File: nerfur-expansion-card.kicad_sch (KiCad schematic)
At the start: 12 parts, among them J1 RJ45, J10 AudioJack4, J11 HDMI_A, J2 Micro_SD_Card, J3 RJ45, J4 Micro_SD_Card, J5 USB_A, J6 USB_A, J7 USB_A, J8 HDMI_A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

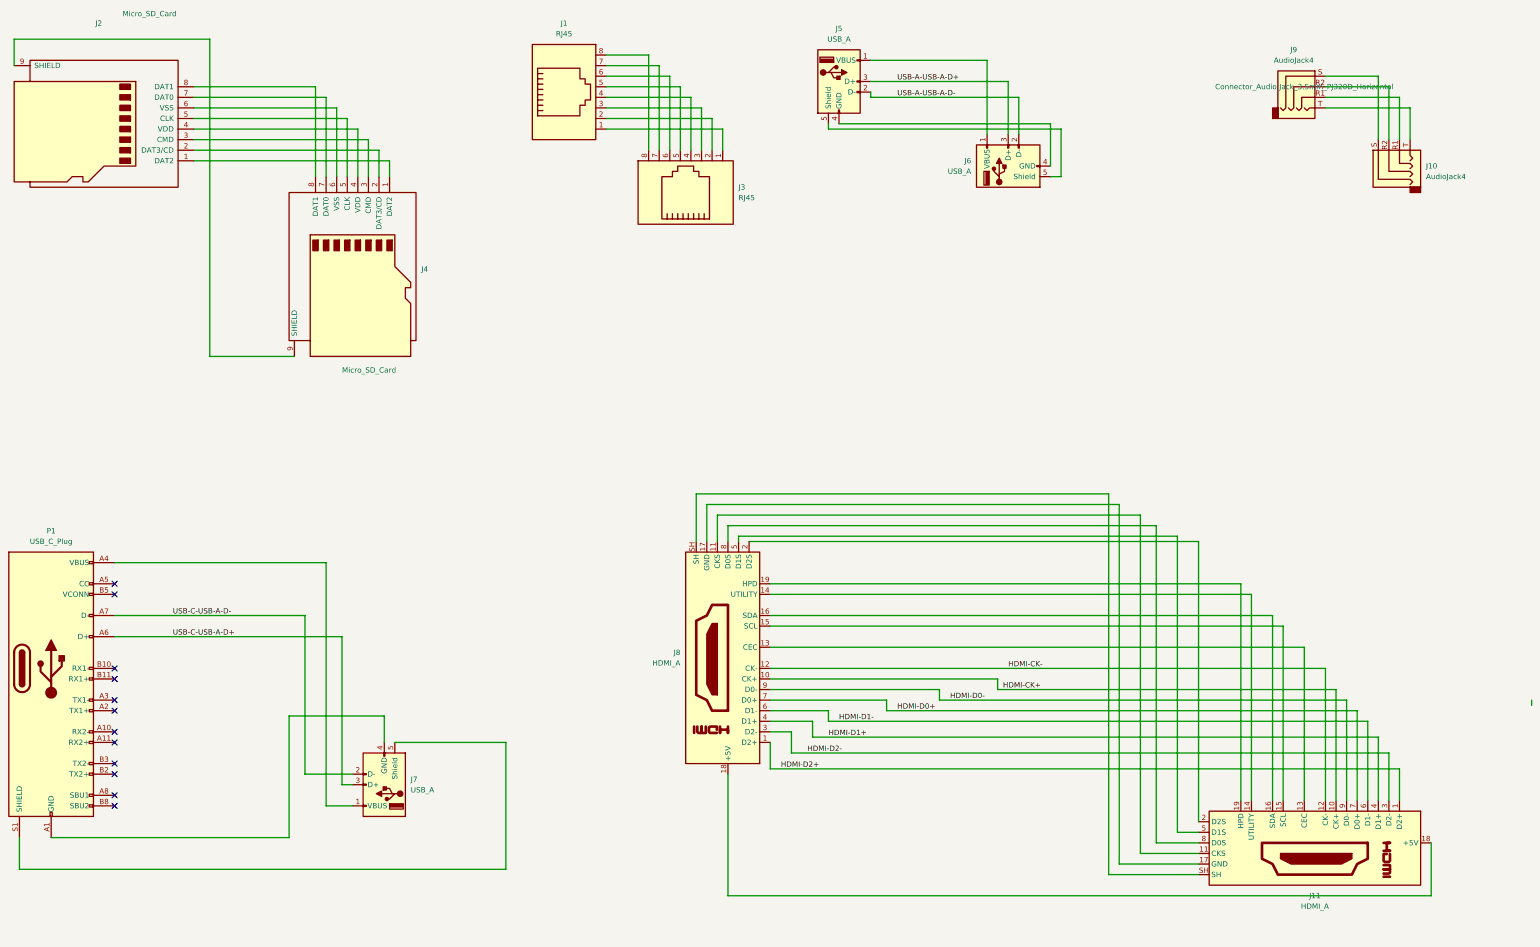
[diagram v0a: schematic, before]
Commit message: kicad-v9 s-expressions
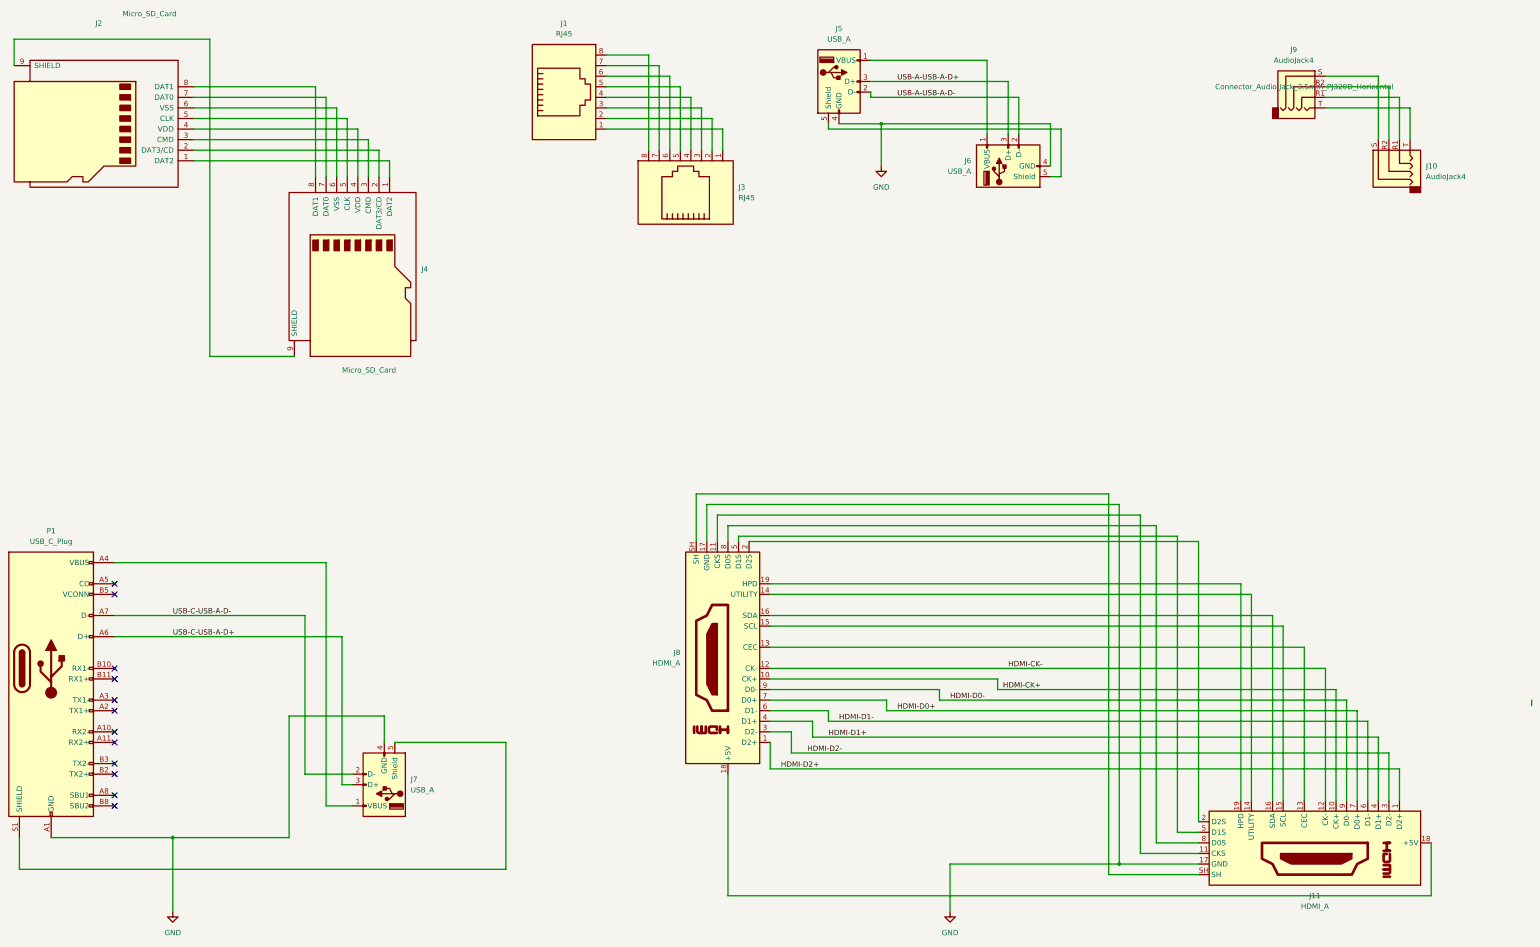
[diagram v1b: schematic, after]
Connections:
- net GND: now reaches J7.4 (GND), P1.A1 (GND), P1.A12 (GND), P1.B1 (GND), P1.B12 (GND)
- net GND: now also J11.17 (GND), J5.4 (GND), J6.4 (GND), J8.17 (GND)

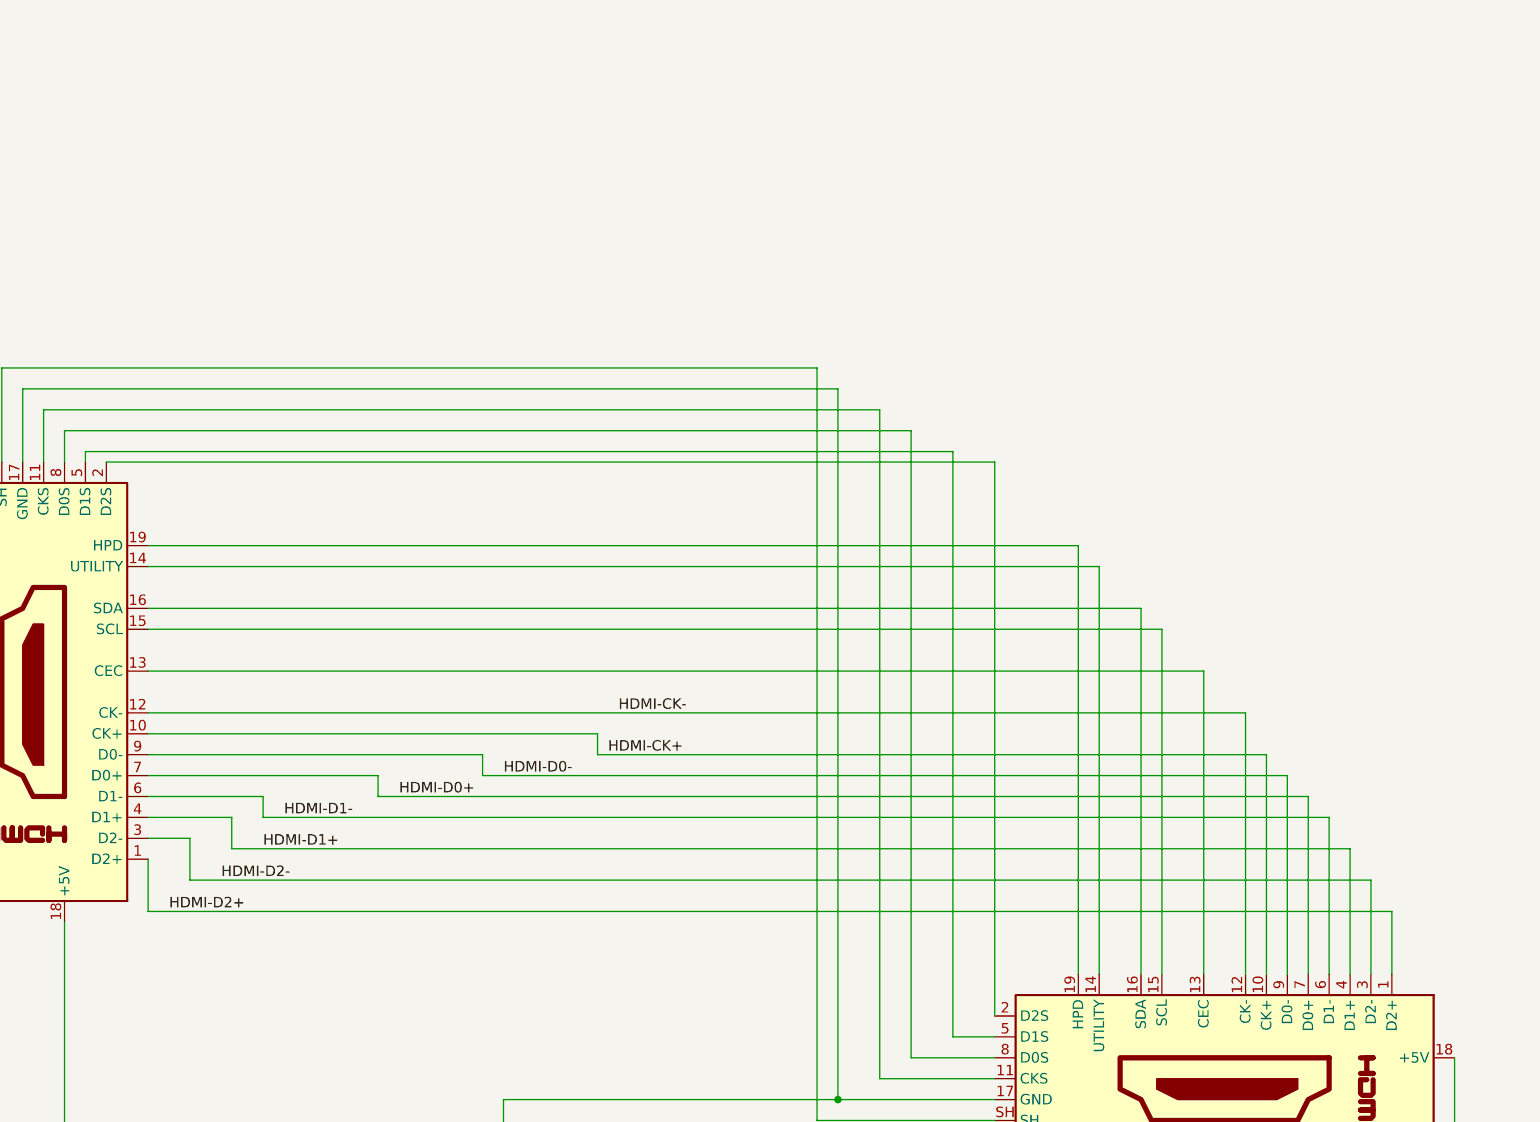
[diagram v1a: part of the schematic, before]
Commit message: schematics: TVS diode arrays on HDMI grounding
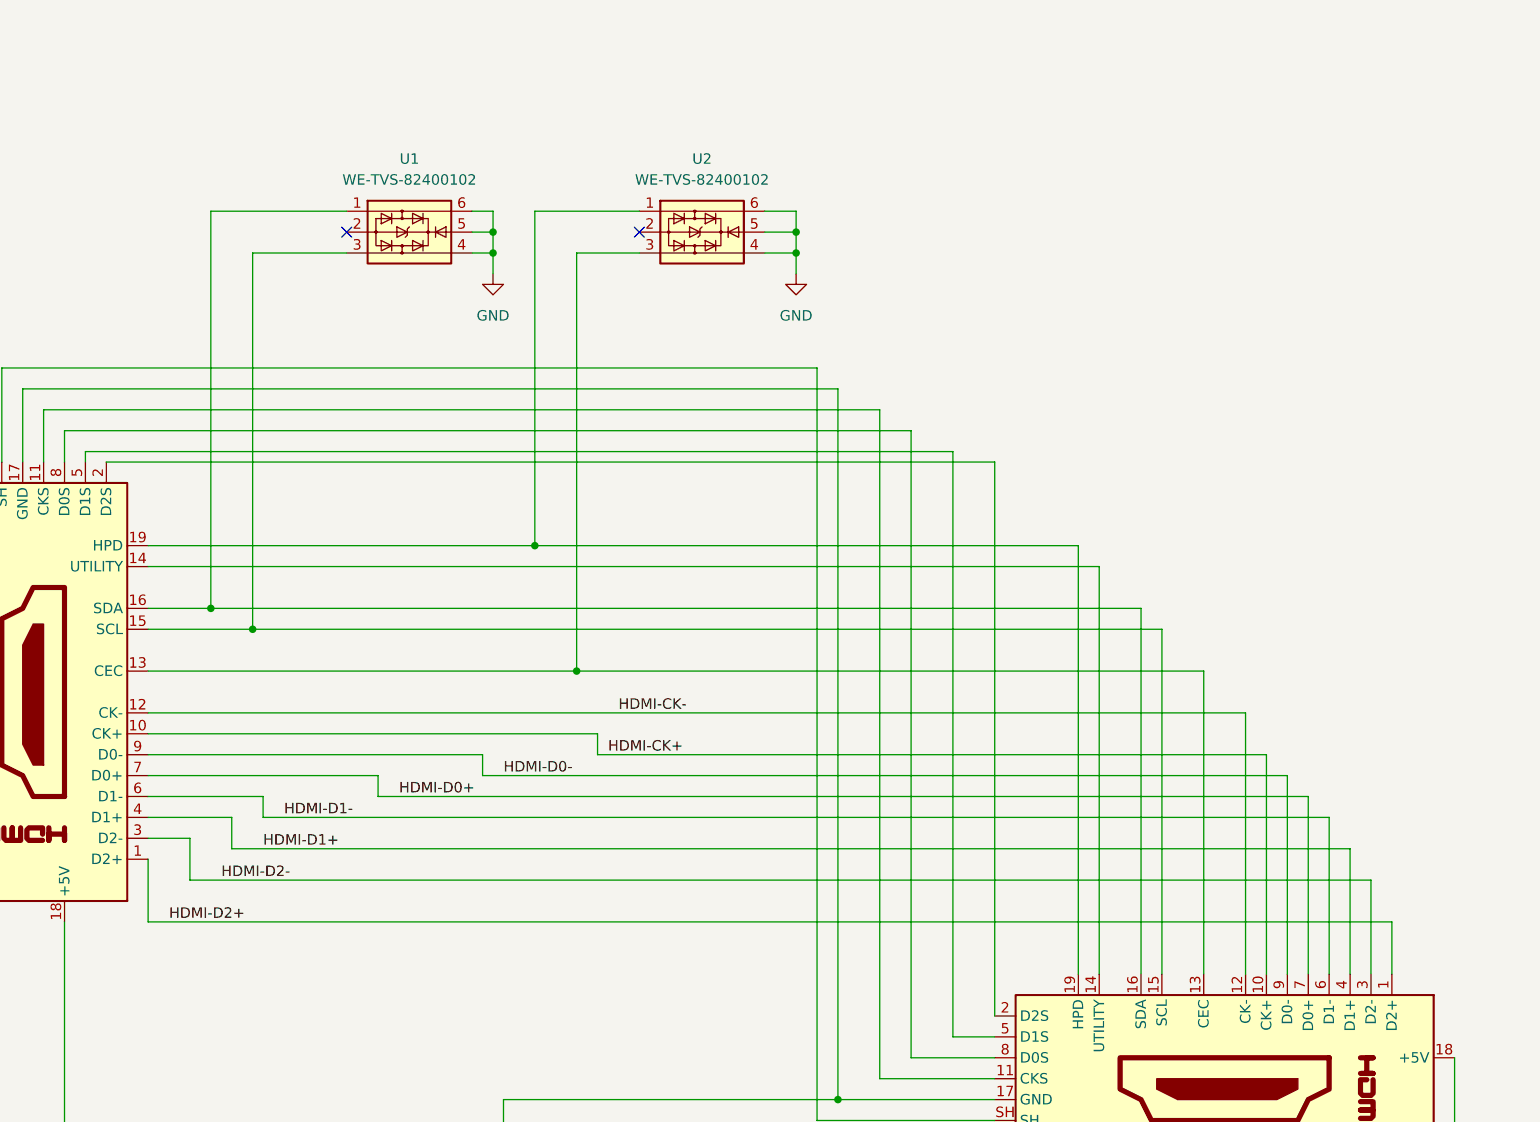
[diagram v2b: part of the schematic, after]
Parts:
- added U1, U2: WE-TVS-82400102, Package_TO_SOT_SMD:SOT-23-6, symbol Power_Protection:WE-TVS-82400102
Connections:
- net GND: now also U1.4, U1.5, U1.6, U2.4, U2.5, U2.6
- net at J11.13 (CEC), J8.13 (CEC): now also U2.3
- net at J11.15 (SCL), J8.15 (SCL): now also U1.3
- net at J11.16 (SDA), J8.16 (SDA): now also U1.1
- net at J11.19 (HPD), J8.19 (HPD): now also U2.1
- no-connect marks 12 -> 14
